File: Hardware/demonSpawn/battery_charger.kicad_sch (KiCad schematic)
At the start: 28 parts, among them U4 BQ25616, U5 TPS61023DRL

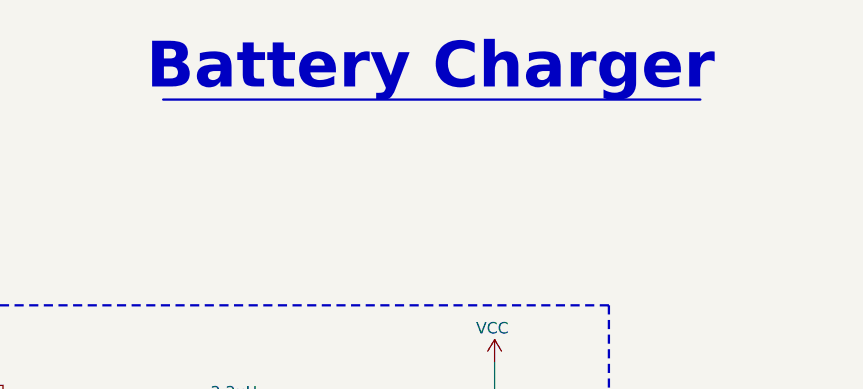
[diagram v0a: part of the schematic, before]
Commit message: doc: Add schematic pdf
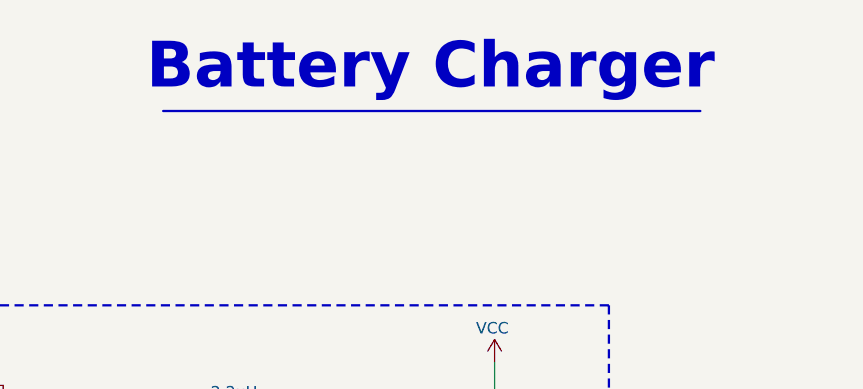
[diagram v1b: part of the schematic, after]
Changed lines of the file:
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@@
 	(polyline
 		(pts
-			(xy 121.92 21.59) (xy 181.61 21.59)
+			(xy 121.92 22.86) (xy 181.61 22.86)
 		)
 		(stroke
